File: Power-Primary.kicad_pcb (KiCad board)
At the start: 2 copper layers, 174 x 72 mm, 53 parts, among them J1 HV in, J10 SPARE, J11 SPARE, J2 Dashboard, J3 Telemetry, J4 Motor, J5 MPPT 1, J6 MPPT 2, J7 BPS, J8 Primary Disconn., J9 SPARE, U1 Mean_Well_12V

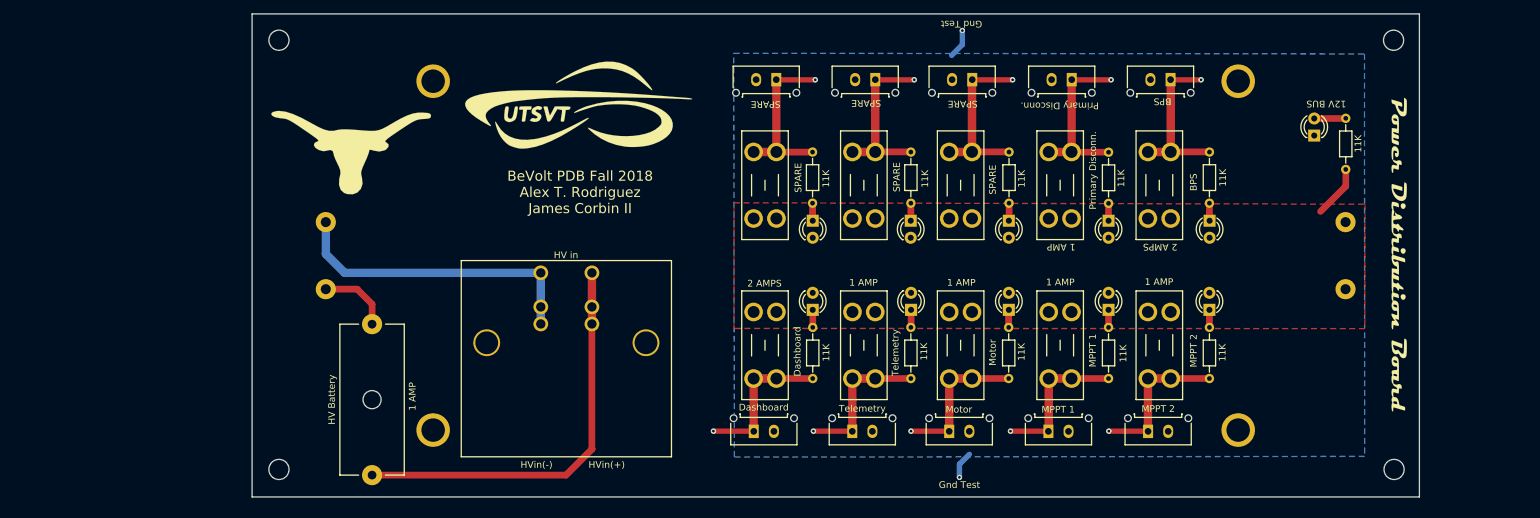
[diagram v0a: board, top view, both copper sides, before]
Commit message: Extend design (#1)
* Practice push + changed schematic

* schematic almost done, connection errors

* schematic done, U1 pin 3/4 error

* finished schematic

* finished PCB waiting for edits

* pcb edits

* fixed component spacing

* refilled zones

* completed Hannah's edits

* Sijin's edits, mounting hole and power planes

* Deletes gerbers from this because added to release and adds dimensions

Co-authored-by: Hannahslee14 <hannahslee@utexas.edu>
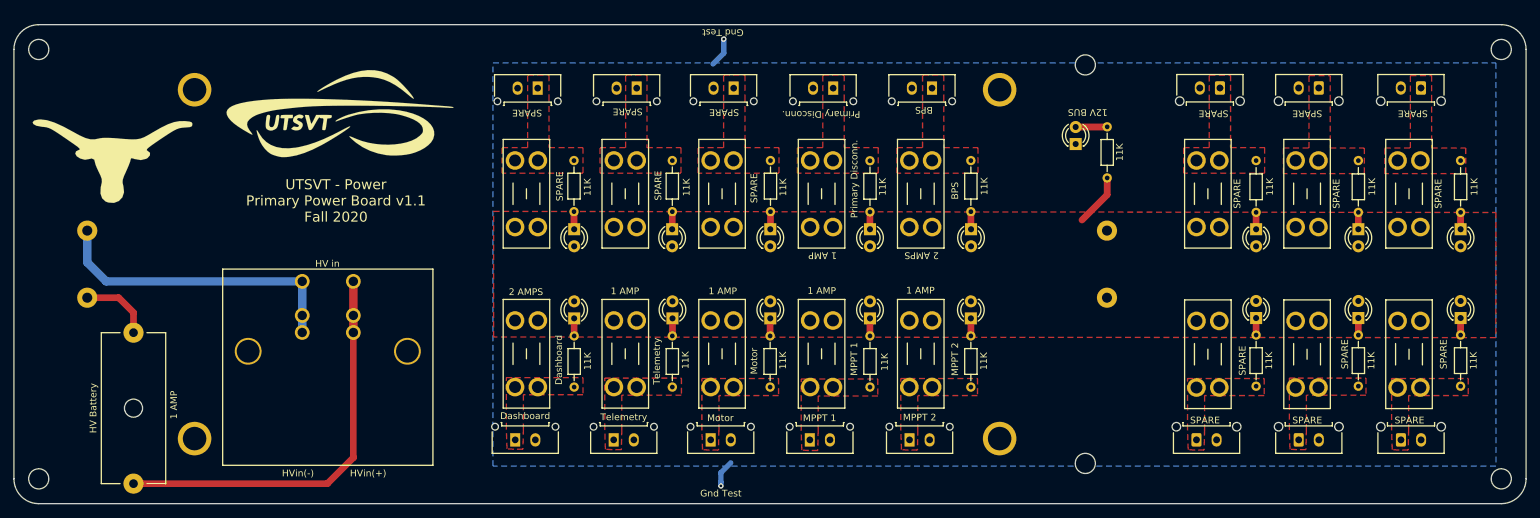
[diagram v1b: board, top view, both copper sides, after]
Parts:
- removed the G*** at (210.3, 104.1)
- removed the REF** at (221.1, 58.9)
- added D11: LED, LED_THT:LED_D3.0mm, F.Cu at (200.7, 100.3)
- added D12: LED, LED_THT:LED_D3.0mm, F.Cu at (215.9, 100.3)
- added D13: LED, LED_THT:LED_D3.0mm, F.Cu at (231.1, 100.3)
- added D14: LED, LED_THT:LED_D3.0mm, F.Cu at (231.1, 87.1)
- added D15: LED, LED_THT:LED_D3.0mm, F.Cu at (215.9, 87.1)
- added D16: LED, LED_THT:LED_D3.0mm, F.Cu at (200.7, 87.1)
- added F12: SPARE, Fuse:Fuseholder_Blade_Mini_Keystone_3568, F.Cu at (195.2, 100.8)
- added F13: SPARE, Fuse:Fuseholder_Blade_Mini_Keystone_3568, F.Cu at (210.0, 100.8)
- added F14: SPARE, Fuse:Fuseholder_Blade_Mini_Keystone_3568, F.Cu at (225.2, 100.8)
- added F15: SPARE, Fuse:Fuseholder_Blade_Mini_Keystone_3568, F.Cu at (221.8, 86.8)
- added F16: SPARE, Fuse:Fuseholder_Blade_Mini_Keystone_3568, F.Cu at (206.6, 86.8)
- added F17: SPARE, Fuse:Fuseholder_Blade_Mini_Keystone_3568, F.Cu at (191.8, 86.8)
- added J12: SPARE, Connector_Molex:Molex_Micro-Fit_3.0_43650-0215_1x02_P3.00mm_Vertical, F.Cu at (191.8, 118.5)
- added J13: SPARE, Connector_Molex:Molex_Micro-Fit_3.0_43650-0215_1x02_P3.00mm_Vertical, F.Cu at (207.0, 118.5)
- added J14: SPARE, Connector_Molex:Molex_Micro-Fit_3.0_43650-0215_1x02_P3.00mm_Vertical, F.Cu at (222.2, 118.5)
- added J15: SPARE, Connector_Molex:Molex_Micro-Fit_3.0_43650-0215_1x02_P3.00mm_Vertical, F.Cu at (225.2, 66.0)
- added J16: SPARE, Connector_Molex:Molex_Micro-Fit_3.0_43650-0215_1x02_P3.00mm_Vertical, F.Cu at (210.0, 66.0)
- added J17: SPARE, Connector_Molex:Molex_Micro-Fit_3.0_43650-0215_1x02_P3.00mm_Vertical, F.Cu at (195.3, 66.0)
- added R11: 11K, Resistor_THT:R_Axial_DIN0204_L3.6mm_D1.6mm_P7.62mm_Horizontal, F.Cu at (200.7, 110.5)
- added R12: 11K, Resistor_THT:R_Axial_DIN0204_L3.6mm_D1.6mm_P7.62mm_Horizontal, F.Cu at (215.9, 110.5)
- added R13: 11K, Resistor_THT:R_Axial_DIN0204_L3.6mm_D1.6mm_P7.62mm_Horizontal, F.Cu at (231.1, 110.5)
- added R14: 11K, Resistor_THT:R_Axial_DIN0204_L3.6mm_D1.6mm_P7.62mm_Horizontal, F.Cu at (231.1, 77.0)
- added R15: 11K, Resistor_THT:R_Axial_DIN0204_L3.6mm_D1.6mm_P7.62mm_Horizontal, F.Cu at (215.9, 77.0)
- added R16: 11K, Resistor_THT:R_Axial_DIN0204_L3.6mm_D1.6mm_P7.62mm_Horizontal, F.Cu at (200.7, 77.0)
- added REF**: MountingHole_3mm, MountingHole:MountingHole_3.7mm, F.Cu at (175.2, 62.6)
- added REF**: MountingHole_3mm, MountingHole:MountingHole_3.7mm, F.Cu at (175.2, 122.0)
- added REF**: MountingHole_3mm, MountingHole:MountingHole_3.7mm, F.Cu at (237.2, 60.3)
- moved REF** 35.8 mm to (19.2, 124.3)
- moved REF** 35.8 mm to (19.2, 60.3)
- moved D9 35.6 mm to (113.6, 89.6)
- moved F3 35.6 mm to (108.3, 100.7)
- moved F4 35.6 mm to (122.8, 100.7)
- moved J1 35.6 mm to (58.5, 94.9)
- moved D17 35.6 mm to (173.8, 74.4)
- moved D3 35.6 mm to (128.2, 97.8)
- moved D4 35.6 mm to (143.1, 97.8)
- moved D5 35.6 mm to (158.1, 97.8)
- moved D6 35.6 mm to (158.2, 89.6)
- moved D7 35.6 mm to (143.1, 89.6)
- moved D8 35.6 mm to (128.2, 89.6)
- moved F10 35.6 mm to (104.9, 86.8)
- moved F5 35.6 mm to (137.6, 100.7)
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- renumbered D11 to D17, R11 to R18
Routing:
- net Net-(F9-Pad2): track 25.8 -> 0.14 mm, vias 1 -> 0
- net Net-(F8-Pad2): track 25.7 -> 0.21 mm, vias 1 -> 0
- net Net-(F11-Pad2): track 25.4 -> 0.12 mm, vias 1 -> 0
- net Net-(F10-Pad2): track 25.3 -> 0.07 mm, vias 1 -> 0
- net Net-(F7-Pad2): track 24.6 -> 0.12 mm, vias 1 -> 0
- net Net-(F6-Pad2): track 22.9 -> 0.12 mm, vias 1 -> 0
- net Net-(F2-Pad2): track 22.7 -> 0.08 mm, vias 1 -> 0
- net Net-(F4-Pad2): track 22.5 -> 0.04 mm, vias 1 -> 0
- net Net-(F5-Pad2): track 22.7 -> 0.30 mm, vias 1 -> 0
- net Net-(F3-Pad2): track 22.4 -> 0.12 mm, vias 1 -> 0
- net Net-(D13-Pad2): track 0.00 -> 2.54 mm
- net Net-(D12-Pad2): track 0.00 -> 2.54 mm
- net Net-(D11-Pad2): track 0.00 -> 2.54 mm
- net Net-(D16-Pad2): track 0.00 -> 2.52 mm
- net Net-(D15-Pad2): track 0.00 -> 2.52 mm
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- added copper zone on F.Cu, net Net-(F10-Pad2)
- added copper zone on F.Cu, net Net-(F11-Pad2)
- added copper zone on F.Cu, net Net-(F12-Pad2)
- added copper zone on F.Cu, net Net-(F13-Pad2)
- added copper zone on F.Cu, net Net-(F14-Pad2)
- added copper zone on F.Cu, net Net-(F15-Pad2)
- added copper zone on F.Cu, net Net-(F16-Pad2)
- added copper zone on F.Cu, net Net-(F17-Pad2)
- added copper zone on F.Cu, net Net-(F2-Pad2)
- added copper zone on F.Cu, net Net-(F3-Pad2)
- added copper zone on F.Cu, net Net-(F4-Pad2)
- added copper zone on F.Cu, net Net-(F5-Pad2)
- added copper zone on F.Cu, net Net-(F6-Pad2)
- added copper zone on F.Cu, net Net-(F7-Pad2)
- added copper zone on F.Cu, net Net-(F8-Pad2)
- added copper zone on F.Cu, net Net-(F9-Pad2)
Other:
- board size 174 x 72 mm -> 225.4 x 71.4 mm
- board text added: "UTSVT - Power Primary Power Board v1.1 Fall 2020"
- board text removed: "BeVolt PDB Fall 2018 Alex T. Rodriguez James Corbin II"

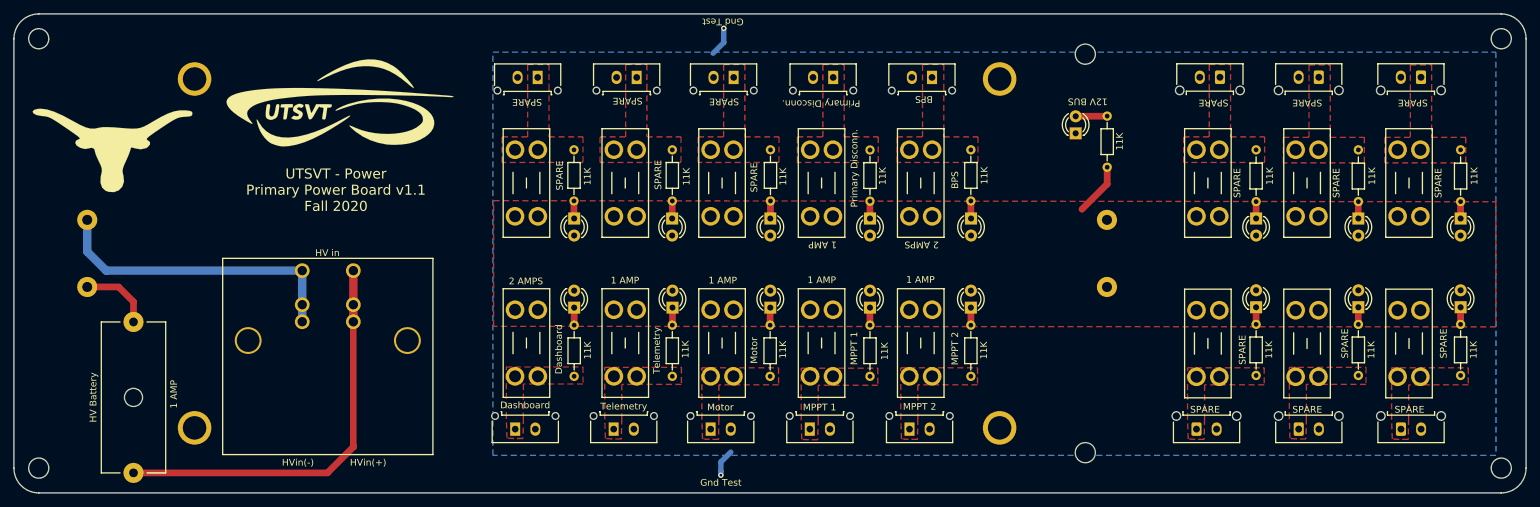
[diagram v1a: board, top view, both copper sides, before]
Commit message: Add STEP files. Some connectors still missing
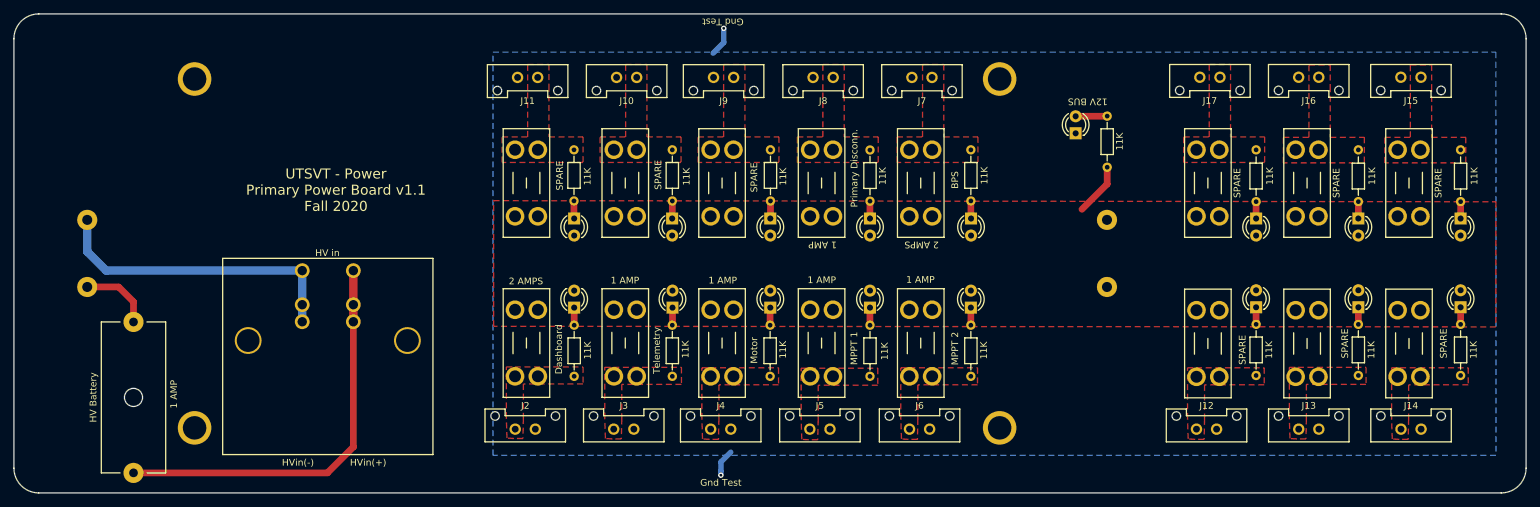
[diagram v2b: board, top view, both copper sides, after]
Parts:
- removed G***: LOGO, Power Board Parts:Longhorn
- removed G***: LOGO, Power Board Parts:Hallock
- removed G***: LOGO, Power Board Parts:Logo
- removed REF** (x6): MountingHole_3mm, MountingHole:MountingHole_3.7mm
- J10, J11, J12, J13, J14, J15, J16, J17, J2, J3, J4, J5, J6, J7, J8, J9: footprint Connector_Molex:Molex_Micro-Fit_3.0_43650-0215_1x02_P3.00mm_Vertical -> UTSVT_Connectors:Molex_MicroFit3.0_1x2xP3.00mm_PolarizingPeg_Vertical
- U1: footprint Power Board Parts:DC-DC Converter 12V -> UTSVT_Power:Mean_Well_12V

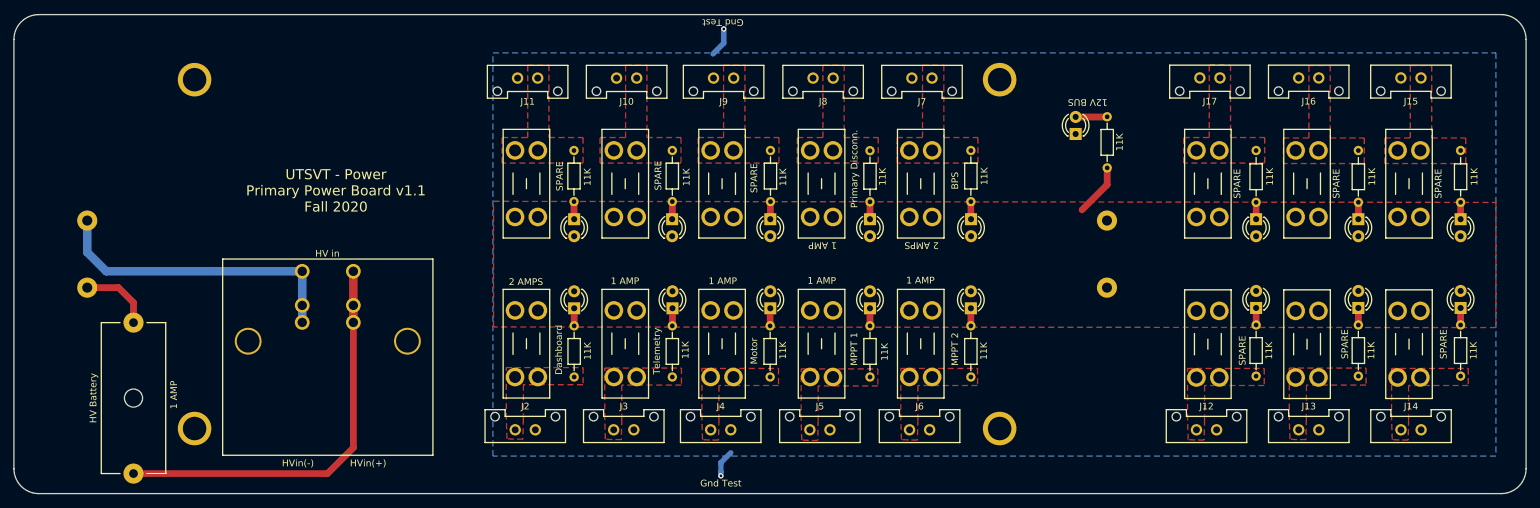
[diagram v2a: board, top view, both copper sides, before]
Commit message: Added mounting holes and updated pcb/sch
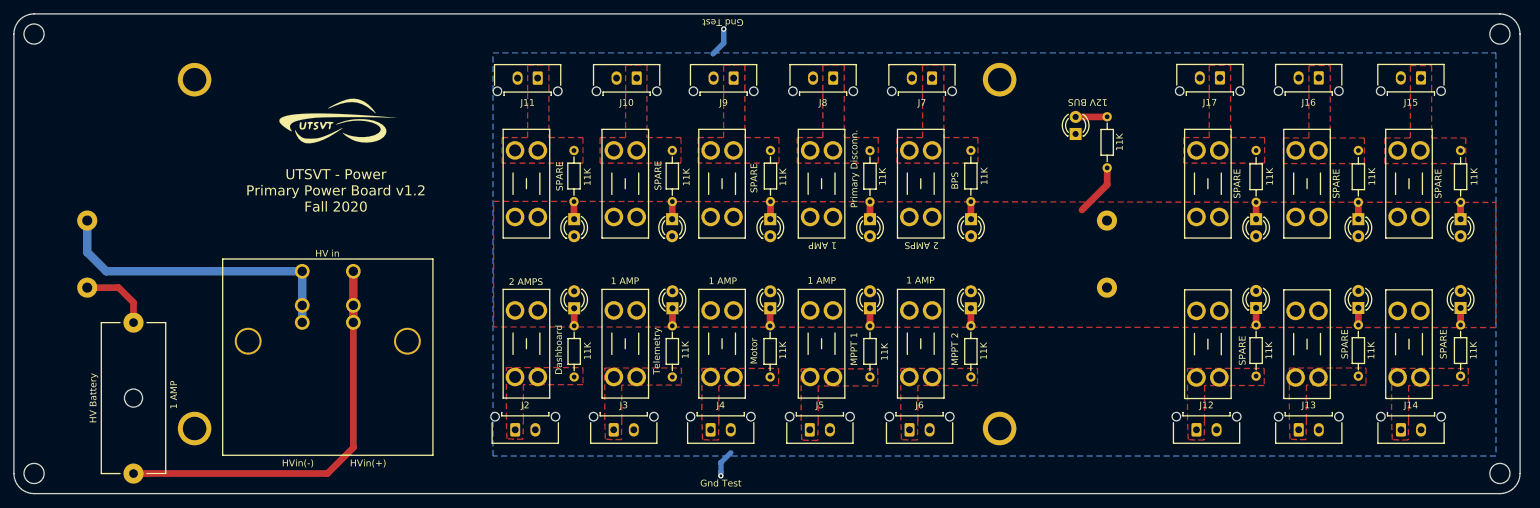
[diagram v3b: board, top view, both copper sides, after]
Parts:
- added H1: MountingHole, MountingHole:MountingHole_3mm, F.Cu at (18.5, 59.5)
- added H2: MountingHole, MountingHole:MountingHole_3mm, F.Cu at (237.0, 59.5)
- added H3: MountingHole, MountingHole:MountingHole_3mm, F.Cu at (18.5, 125.0)
- added H4: MountingHole, MountingHole:MountingHole_3mm, F.Cu at (237.0, 125.0)
- added LOGO1: Logo, UTSVT_Special:UTSVT_Logo_Symbol, F.Cu at (63.5, 72.6)
- added LOGO2: Hallock, UTSVT_Special:Hallock_Image, B.Cu at (61.9, 77.4)
- J10, J11, J12, J13, J14, J15, J16, J17, J2, J3, J4, J5, J6, J7, J8, J9: footprint UTSVT_Connectors:Molex_MicroFit3.0_1x2xP3.00mm_PolarizingPeg_Vertical -> Connector_Molex:Molex_Micro-Fit_3.0_43650-0215_1x02_P3.00mm_Vertical
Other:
- board size 225.4 x 71.4 mm -> 224.5 x 71.5 mm
- board text added: "UTSVT - Power Primary Power Board v1.2 Fall 2020"
- board text removed: "UTSVT - Power Primary Power Board v1.1 Fall 2020"

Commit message: Adds gerbers and gets rid of binding labels
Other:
- board text removed: "2 AMPS"
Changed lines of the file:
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@@
   (general
     (thickness 1.6)
-    (drawings 29)
+    (drawings 22)
     (tracks 95)
     (zones 0)
@@
       (effects (font (size 1 1) (thickness 0.15)))
     )
-    (fp_text value SPARE (at 4.96 6.07 90) (layer F.SilkS)
+    (fp_text value SPARE (at 5.6664 6.43 90) (layer F.SilkS) hide
       (effects (font (size 1 1) (thickness 0.15)))
     )
@@
       (effects (font (size 1 1) (thickness 0.15)))
     )
-    (fp_text value SPARE (at 4.96 6.07 90) (layer F.SilkS)
+    (fp_text value SPARE (at 5.6664 6.4474 90) (layer F.SilkS) hide
       (effects (font (size 1 1) (thickness 0.15)))
     )
@@
       (effects (font (size 1 1) (thickness 0.15)))
     )
-    (fp_text value SPARE (at 4.96 6.07 90) (layer F.SilkS)
+    (fp_text value SPARE (at 5.6664 6.45 90) (layer F.SilkS) hide
       (effects (font (size 1 1) (thickness 0.15)))
     )
@@
       (effects (font (size 1 1) (thickness 0.15)))
     )
-    (fp_text value SPARE (at 4.96 -3.45 90) (layer F.SilkS)
+    (fp_text value SPARE (at 4.2336 -3.05 90) (layer F.SilkS) hide
       (effects (font (size 1 1) (thickness 0.15)))
     )
@@
       (effects (font (size 1 1) (thickness 0.15)))
     )
-    (fp_text value SPARE (at 4.96 -3.95 90) (layer F.SilkS)
+    (fp_text value SPARE (at 4.2336 -3.0474 90) (layer F.SilkS) hide
       (effects (font (size 1 1) (thickness 0.15)))
     )
@@
       (effects (font (size 1 1) (thickness 0.15)))
     )
-    (fp_text value SPARE (at 5.9136 -3.45 90) (layer F.SilkS)
+    (fp_text value SPARE (at 4.2336 -3.03 90) (layer F.SilkS) hide
       (effects (font (size 1 1) (thickness 0.15)))
     )
@@
       (effects (font (size 1 1) (thickness 0.15)))
     )
-    (fp_text value SPARE (at 5.7912 6.477 90) (layer F.SilkS)
+    (fp_text value SPARE (at 6.0664 6.477 90) (layer F.SilkS) hide
       (effects (font (size 1 1) (thickness 0.15)))
     )
@@
       (effects (font (size 1 1) (thickness 0.15)))
     )
-    (fp_text value SPARE (at 6.1722 6.604 90) (layer F.SilkS)
+    (fp_text value SPARE (at 6.0664 6.4726 90) (layer F.SilkS) hide
       (effects (font (size 1 1) (thickness 0.15)))
     )
@@
       (effects (font (size 1 1) (thickness 0.15)))
     )
-    (fp_text value Dashboard (at 5.8801 -3.1278 270) (layer F.SilkS)
+    (fp_text value Dashboard (at 5.8801 -3.1278 270) (layer F.SilkS) hide
       (effects (font (size 1 1) (thickness 0.15)))
     )
@@
       (effects (font (size 1 1) (thickness 0.15)))
     )
-    (fp_text value Telemetry (at 6.0579 -3.0008 270) (layer F.SilkS)
+    (fp_text value Telemetry (at 6.0579 -3.0008 270) (layer F.SilkS) hide
       (effects (font (size 1 1) (thickness 0.15)))
     )
@@
       (effects (font (size 1 1) (thickness 0.15)))
     )
-    (fp_text value Motor (at 6.0579 -3.077 270) (layer F.SilkS)
+    (fp_text value Motor (at 6.0579 -3.077 270) (layer F.SilkS) hide
       (effects (font (size 1 1) (thickness 0.15)))
     )
@@
       (effects (font (size 1 1) (thickness 0.15)))
     )
-    (fp_text value "MPPT 1" (at 5.7531 -3.153 270) (layer F.SilkS)
+    (fp_text value "MPPT 1" (at 5.7531 -3.153 270) (layer F.SilkS) hide
       (effects (font (size 1 1) (thickness 0.15)))
     )
@@
       (effects (font (size 1 1) (thickness 0.15)))
     )
-    (fp_text value "MPPT 2" (at 5.7785 -3.4072 90 unlocked) (layer F.SilkS)
+    (fp_text value "MPPT 2" (at 5.7785 -3.4072 90 unlocked) (layer F.SilkS) hide
       (effects (font (size 1 1) (thickness 0.15)))
     )
@@
       (effects (font (size 1 1) (thickness 0.15)))
     )
-    (fp_text value BPS (at 5.4102 6.8072 90) (layer F.SilkS)
+    (fp_text value BPS (at 5.4102 6.8072 90) (layer F.SilkS) hide
       (effects (font (size 1 1) (thickness 0.15)))
     )
@@
       (effects (font (size 1 1) (thickness 0.15)))
     )
-    (fp_text value "Primary Disconn." (at 7.1628 6.5784 90) (layer F.SilkS)
+    (fp_text value "Primary Disconn." (at 6.1664 6.4116 90) (layer F.SilkS) hide
       (effects (font (size 1 1) (thickness 0.15)))
     )
@@
       (effects (font (size 1 1) (thickness 0.15)))
     )
-    (fp_text value SPARE (at 6.0706 6.6548 90) (layer F.SilkS)
+    (fp_text value SPARE (at 4.9664 6.4046 90) (layer F.SilkS) hide
       (effects (font (size 1 1) (thickness 0.15)))
     )
@@
   (gr_line (start 18.5 56.5) (end 237 56.5) (layer Edge.Cuts) (width 0.15))
   (gr_line (start 15.5 59.5) (end 15.5 125) (layer Edge.Cuts) (width 0.15))
-  (gr_text "1 AMP" (at 136.0424 91.0082 180) (layer F.SilkS)
-    (effects (font (size 1 1) (thickness 0.15)))
-  )
-  (gr_text "1 AMP" (at 150.622 96.2152) (layer F.SilkS)
-    (effects (font (size 1 1) (thickness 0.15)))
-  )
-  (gr_text "1 AMP" (at 135.9154 96.266) (layer F.SilkS)
-    (effects (font (size 1 1) (thickness 0.15)))
-  )
-  (gr_text "1 AMP" (at 106.5784 96.3168) (layer F.SilkS)
-    (effects (font (size 1 1) (thickness 0.15)))
-  )
-  (gr_text "2 AMPS" (at 91.821 96.4438) (layer F.SilkS)
-    (effects (font (size 1 1) (thickness 0.15)))
-  )
-  (gr_text "1 AMP" (at 121.158 96.3168) (layer F.SilkS)
-    (effects (font (size 1 1) (thickness 0.15)))
-  )
-  (gr_text "2 AMPS" (at 150.7998 91.0082 180) (layer F.SilkS)
-    (effects (font (size 1 1) (thickness 0.15)))
-  )
   (gr_text "1 AMP" (at 39.3446 113.284 90) (layer F.SilkS)
     (effects (font (size 1 1) (thickness 0.15)))
@@
     (effects (font (size 1 1) (thickness 0.15)))
   )
-  (gr_text "Dr. Gary Hallock" (at 80.4926 78.0542 90) (layer B.SilkS)
-    (effects (font (size 1.5 1.5) (thickness 0.3)) (justify mirror))
+  (gr_text "Dr. Gary Hallock" (at 80.4 78.9 90) (layer B.SilkS)
+    (effects (font (size 2 2) (thickness 0.3)) (justify mirror))
   )
   (gr_text "Vin(+)" (at 33.2994 97.155) (layer B.SilkS)
